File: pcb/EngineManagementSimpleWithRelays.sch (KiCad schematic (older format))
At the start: 81 parts, among them P1 VPButtons, P10 VP ButtonPlug, P11 BatteryFused5A, P12 12VSwitched, P13 OnOffTrigger, P14 12vSwitchedIn, P15 0v, P16 Buzzer, P17 Neutral-, P18 Neutral+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

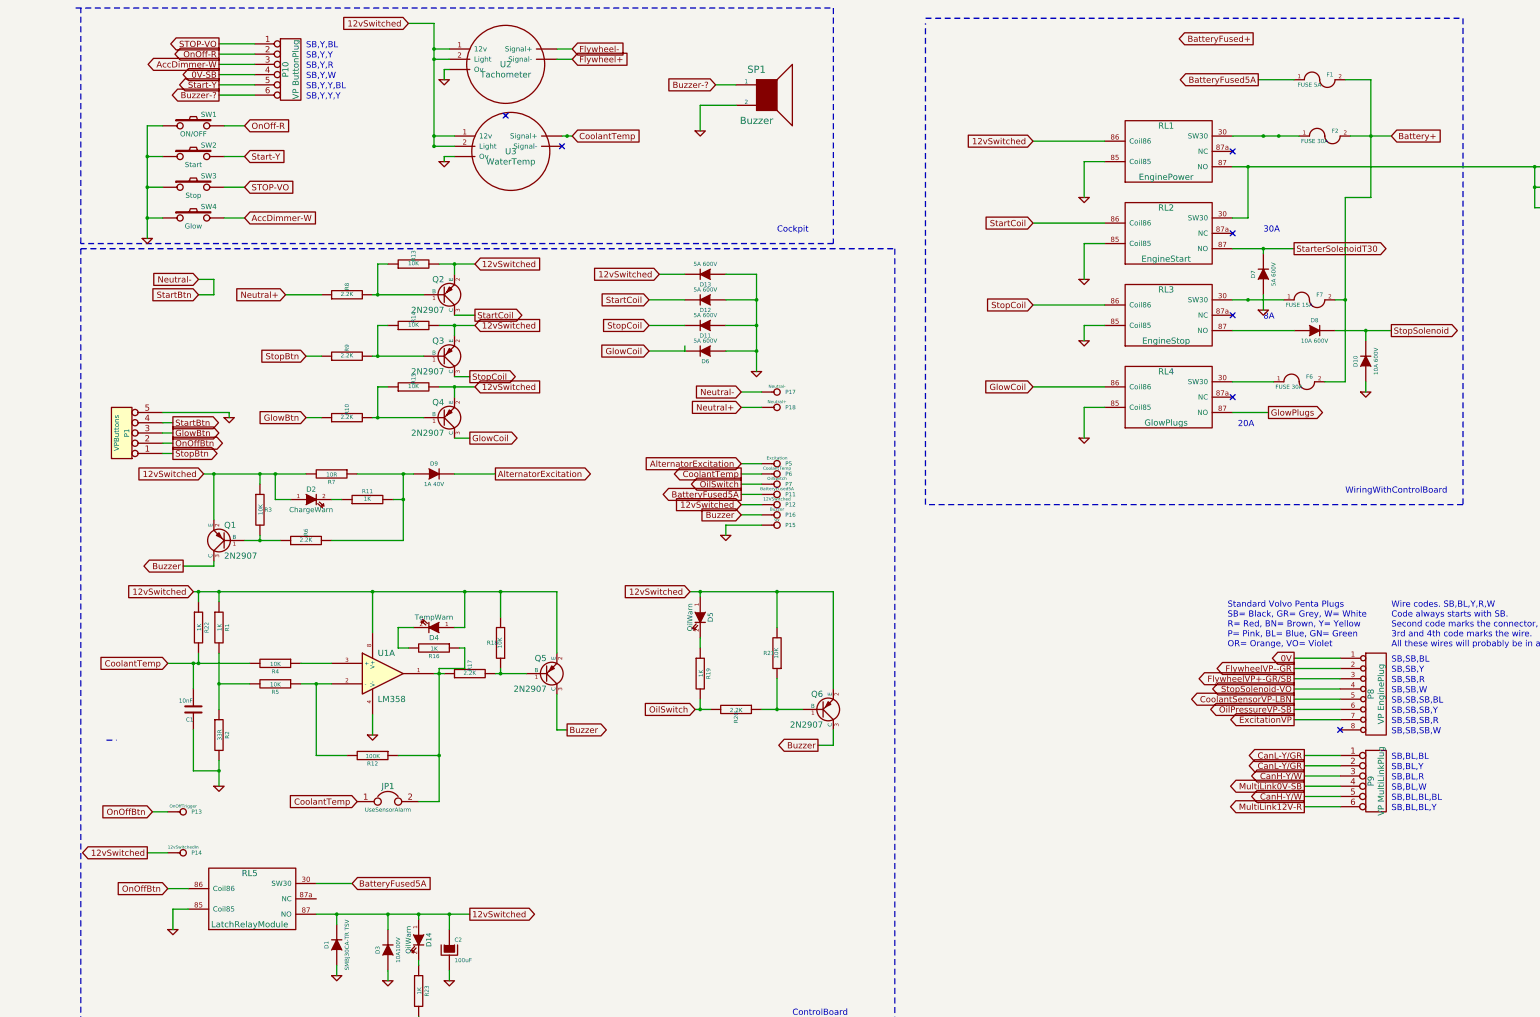
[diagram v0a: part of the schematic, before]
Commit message: Redesigned to not use VP J1939 instruments
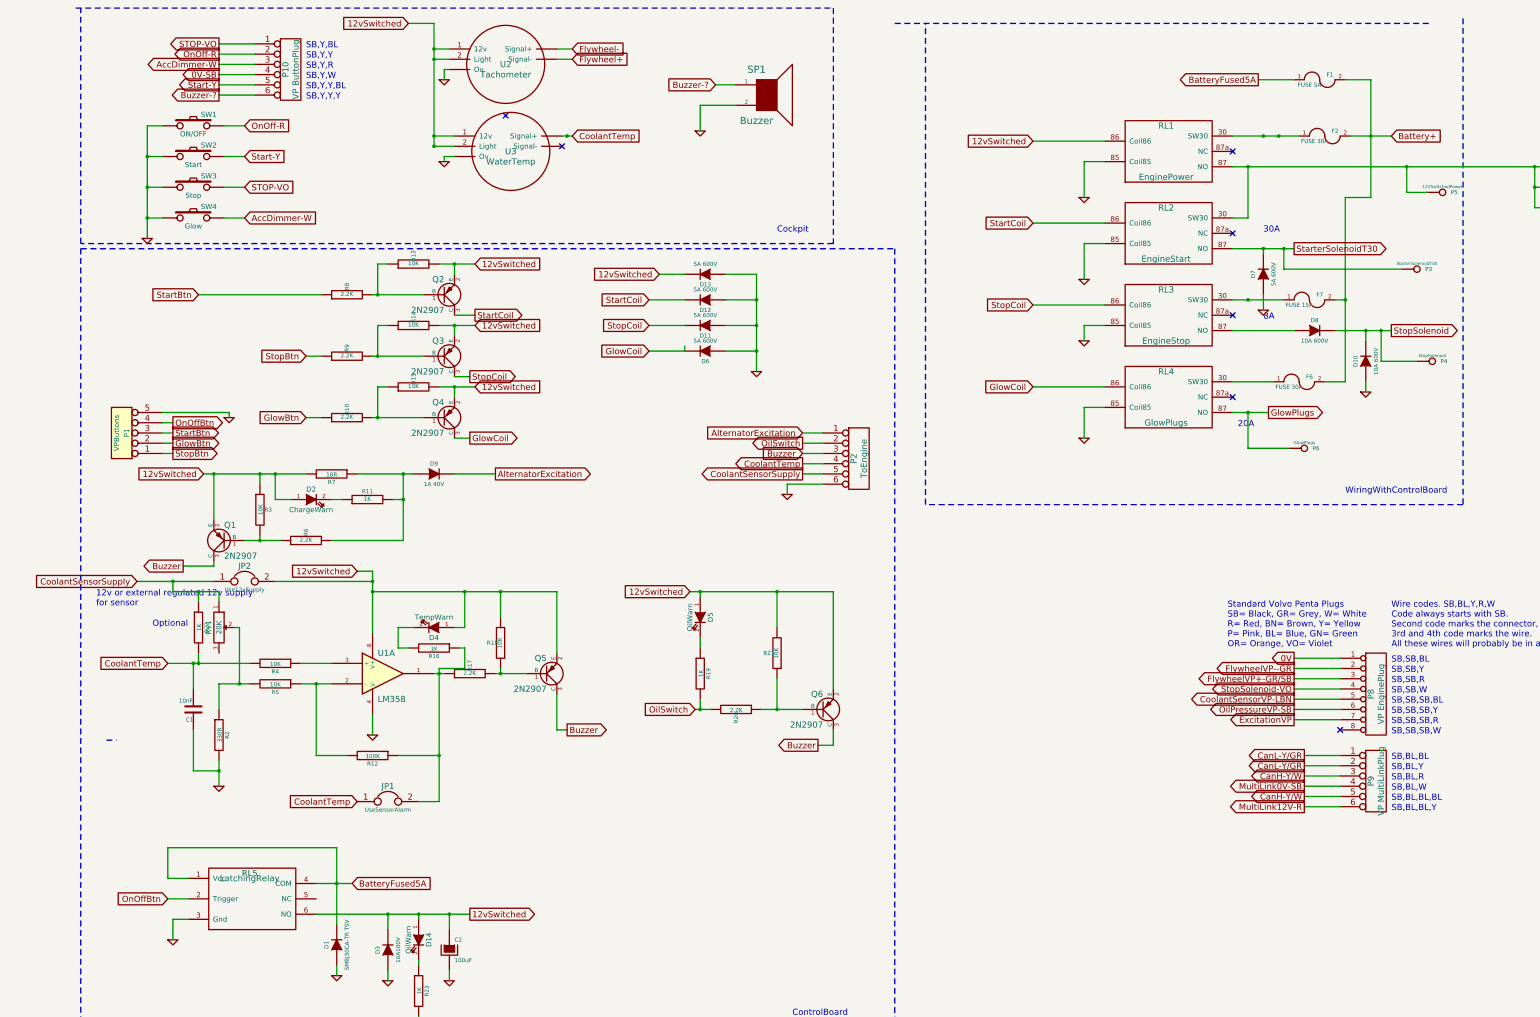
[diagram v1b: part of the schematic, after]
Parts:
- removed P11: BatteryFused5A, Divers:CrimpBlade, symbol CONN_1
- removed P12: 12VSwitched, Divers:CrimpBlade, symbol CONN_1
- removed P13: OnOffTrigger, Divers:CrimpBlade, symbol CONN_1
- removed P14: 12vSwitchedIn, Divers:CrimpBlade, symbol CONN_1
- removed P15: 0v, Divers:CrimpBlade, symbol CONN_1
- removed P16: Buzzer, Divers:CrimpBlade, symbol CONN_1
- removed P17: Neutral-, Divers:CrimpBlade, symbol CONN_1
- removed P18: Neutral+, Divers:CrimpBlade, symbol CONN_1
- removed P7: OilSwitch, Divers:CrimpBlade, symbol CONN_1
- removed R1: 1K, Resistors_SMD:R_0805_HandSoldering, symbol R
- removed RL5: LatchRelayModule, symbol AutomotiveRelay
- added JP2: Use12vSupply, Pin_Headers:Pin_Header_Straight_1x02, symbol JUMPER
- added P2: ToEngine, Connect:bornier6, symbol CONN_6
- added P3: StarterSolenoidT30, Divers:CrimpBlade, symbol CONN_1
- added P4: StopSolenoid, Divers:CrimpBlade, symbol CONN_1
- added RL5: LatchingRelay, Divers:LatchingRelay, symbol LatchingRelay
- added RV1: 20K, Potentiometers:Potentiometer_Bourns_3296W_3-8Zoll_Inline_ScrewUp, symbol POT
- F1, F2, F6, F7: footprint Fuse_Holders_and_Fuses:BladeFuse-Mini -> Divers:UniversalFuseHolder
- JP1: footprint (none) -> Pin_Headers:Pin_Header_Straight_1x02
- P5: value Excitation -> 12VSwitchedPower
- P6: value CoolantTemp -> GlowPlugs
- R2: value 33R -> 330R
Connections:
- net Neutral- is gone; now on net OnOffBtn: P1.4
- net 12vSwitched: now also JP2.2, RL5.6 (NO); no longer D1.2 (K), R22.1
- net AlternatorExcitation: now also P2.1; no longer P5.1
- net BatteryFused5A: now also D1.2 (K), RL5.1 (Vcc), RL5.4 (COM)
- net Buzzer: now also P2.3
- net CoolantTemp: now also P2.4; no longer P6.1
- net GND: now also P2.6, RL5.3 (Gnd)
- net GlowBtn: now also P1.2; no longer P1.3
- net GlowPlugs: now also P6.1
- net OilSwitch: now also P2.2
- net OnOffBtn: now also RL5.2 (Trigger); no longer P1.2
- net StarterSolenoidT30: now also P3.1
- net StopSolenoid: now also P4.1
- net at F3.1, F4.1, F5.1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: now also P5.1
- net at R2.1, R5.2: now also RV1.2
- net Neutral+ renamed StartBtn
- net StartBtn: now also P1.3
- new net CoolantSensorSupply: JP2.1, P2.5, R22.1, RV1.1
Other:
- note added: "12v or external regulated 12v supply\nfor sensor"
- note added: "Optional"

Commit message: Added mosfet based board
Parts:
- R12: value 100K -> 10M
- R17: value 2.2K -> 10K
- R18: value 10K -> 2.2K
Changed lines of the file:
@@
 LIBS:contrib
 LIBS:valves
+LIBS:EngineManagementSimpleWithRelays-cache
 EELAYER 25 0
 EELAYER END
@@
 P 5150 7000
 F 0 "R18" H 5230 7000 40  0000 C CNN
-F 1 "10K" V 5157 7001 40  0000 C CNN
+F 1 "2.2K" V 5157 7001 40  0000 C CNN
 F 2 "Resistors_SMD:R_0805_HandSoldering" V 5080 7000 30  0001 C CNN
 F 3 "" H 5150 7000 30  0000 C CNN
@@
 P 4850 7300
 F 0 "R17" H 4930 7300 40  0000 C CNN
-F 1 "2.2K" V 4857 7301 40  0000 C CNN
+F 1 "10K" V 4857 7301 40  0000 C CNN
 F 2 "Resistors_SMD:R_0805_HandSoldering" V 4780 7300 30  0001 C CNN
 F 3 "" H 4850 7300 30  0000 C CNN
@@
 P 3900 8100
 F 0 "R12" V 3980 8100 40  0000 C CNN
-F 1 "100K" V 3907 8101 40  0000 C CNN
+F 1 "10M" V 3907 8101 40  0000 C CNN
 F 2 "Resistors_SMD:R_0805_HandSoldering" V 3830 8100 30  0001 C CNN
 F 3 "" H 3900 8100 30  0000 C CNN
